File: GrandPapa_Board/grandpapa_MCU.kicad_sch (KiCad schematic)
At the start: 19 parts, among them J6 Conn_02x06, U10 MCP2515, U8 PIC18F26K83, Y1 12MHz

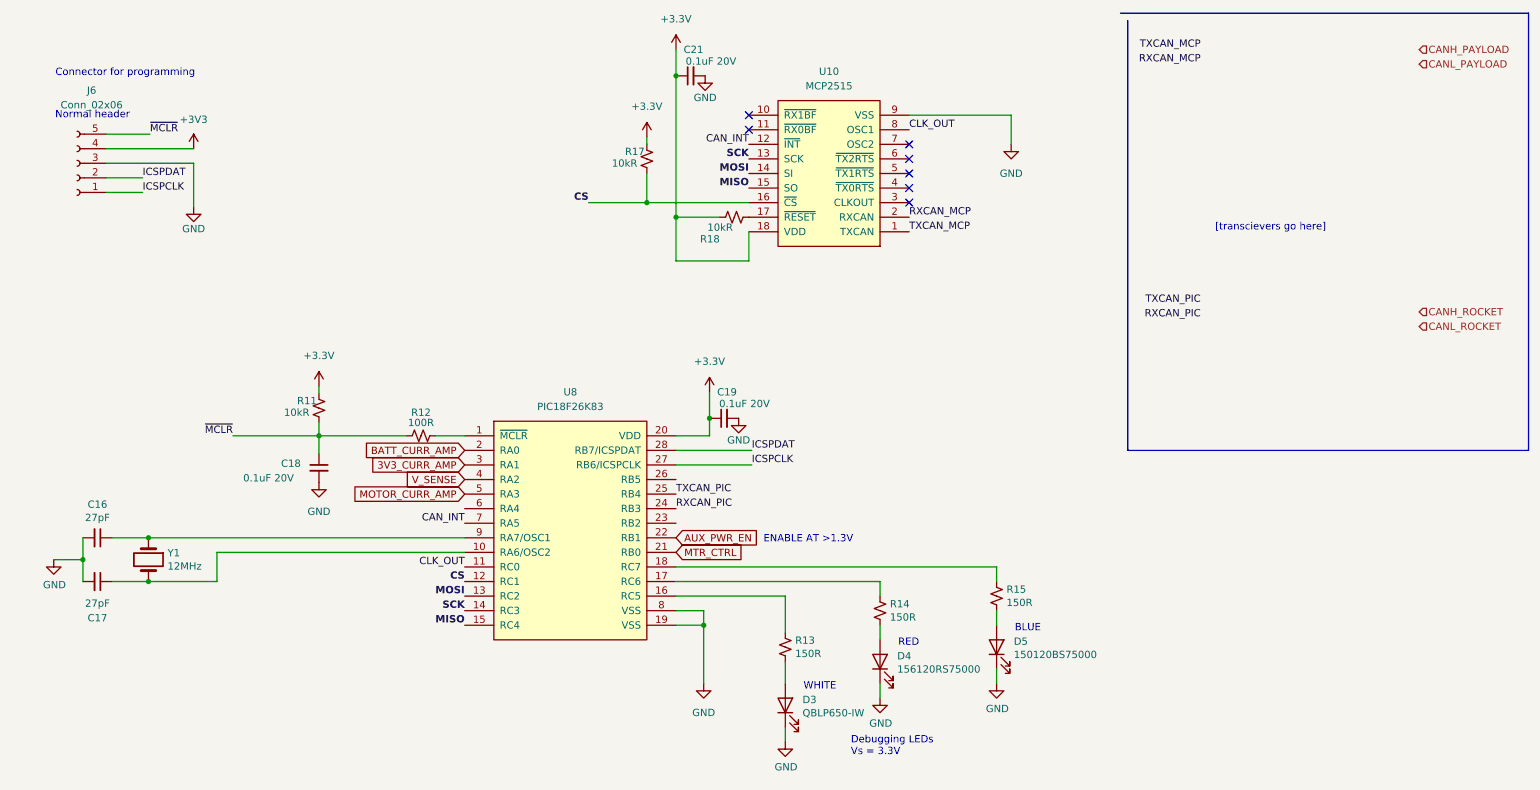
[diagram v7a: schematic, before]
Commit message: clean up schematic, edit nets for clarification, add gnd test points, edit load switching scheme
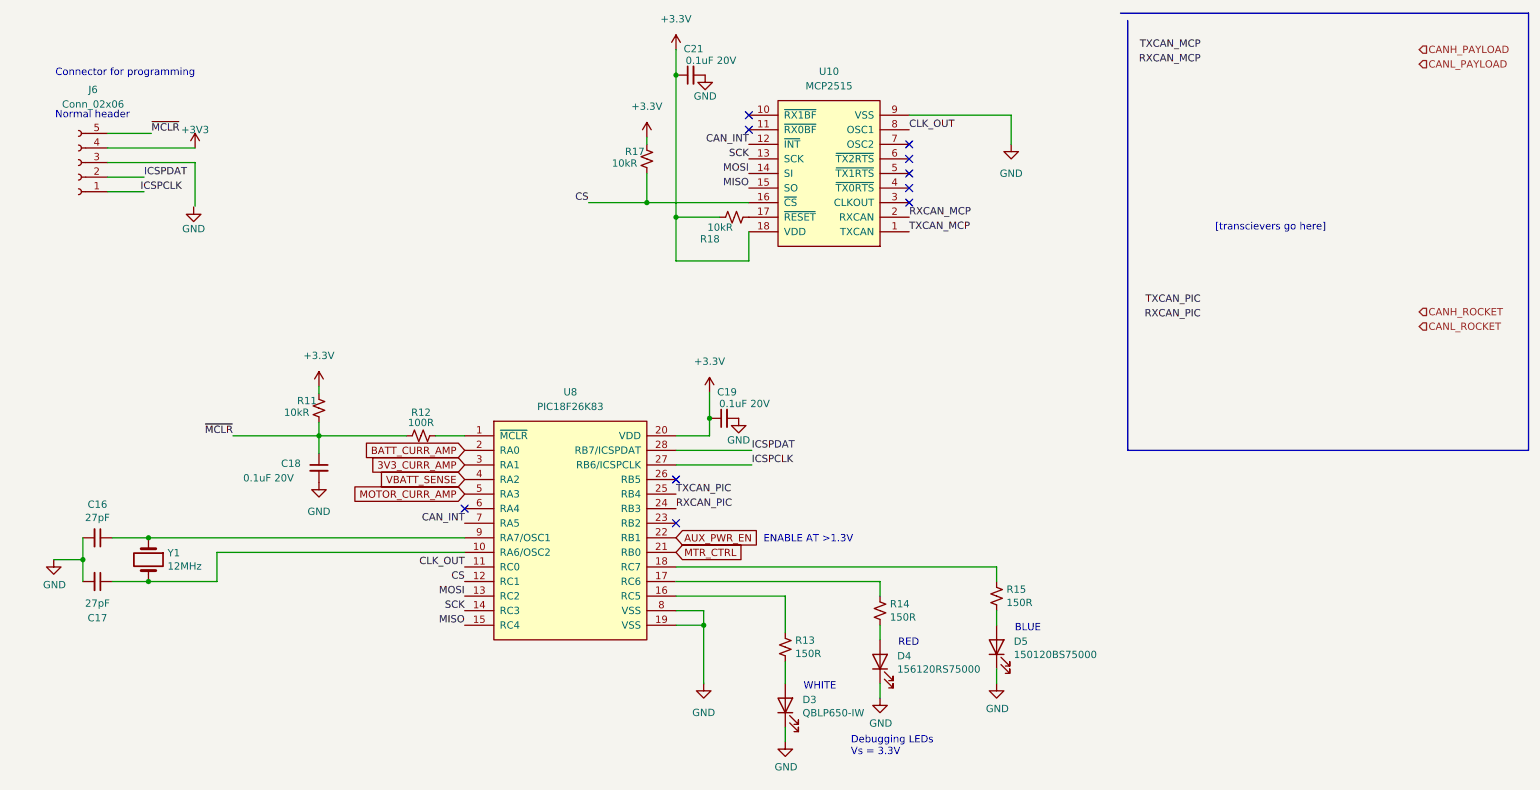
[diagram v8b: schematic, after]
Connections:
- net GND: no longer J6.3 (Pin_3)
- net V_SENSE renamed VBATT_SENSE
- no-connect marks 7 -> 10
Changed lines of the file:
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@@
   (junction (at 137.922 98.552) (diameter 0) (color 0 0 0 0)
   )
-  (junction (at 132.08 38.862) (diameter 0) (color 0 0 0 0)
+  (junction (at 132.08 38.735) (diameter 0) (color 0 0 0 0)
   )
   (junction (at 69.85 101.6) (diameter 0) (color 0 0 0 0)
@@
   (no_connect (at 172.72 58.42))
   (no_connect (at 172.72 60.96))
+  (no_connect (at 132.08 109.22))
+  (no_connect (at 132.08 116.84))
+  (no_connect (at 95.25 114.3))
   (wire (pts (xy 69.85 92.964) (xy 69.85 94.234))
     (stroke (width 0) (type default) (color 0 0 0 0))
@@
     (stroke (width 0) (type default) (color 0 0 0 0))
   )
-  (wire (pts (xy 32.766 49.022) (xy 40.386 49.022))
+  (wire (pts (xy 33.02 48.895) (xy 40.64 48.895))
     (stroke (width 0) (type default) (color 0 0 0 0))
   )
@@
     (stroke (width 0) (type default) (color 0 0 0 0))
   )
-  (wire (pts (xy 32.766 59.182) (xy 39.116 59.182))
+  (wire (pts (xy 33.02 59.055) (xy 39.37 59.055))
     (stroke (width 0) (type default) (color 0 0 0 0))
   )
@@
     (stroke (width 0) (type default) (color 0 0 0 0))
   )
-  (wire (pts (xy 32.766 56.642) (xy 39.116 56.642))
+  (wire (pts (xy 33.02 56.515) (xy 39.37 56.515))
     (stroke (width 0) (type default) (color 0 0 0 0))
   )
@@
     (stroke (width 0) (type default) (color 0 0 0 0))
   )
-  (wire (pts (xy 132.08 38.862) (xy 132.08 63.5))
+  (wire (pts (xy 132.08 38.735) (xy 132.08 63.5))
     (stroke (width 0) (type default) (color 0 0 0 0))
   )
@@
     (stroke (width 0) (type default) (color 0 0 0 0))
   )
-  (wire (pts (xy 48.006 54.102) (xy 48.006 61.722))
+  (wire (pts (xy 48.26 53.975) (xy 48.26 61.595))
     (stroke (width 0) (type default) (color 0 0 0 0))
   )
@@
     (stroke (width 0) (type default) (color 0 0 0 0))
   )
-  (wire (pts (xy 132.08 34.29) (xy 132.08 38.862))
-    (stroke (width 0) (type default) (color 0 0 0 0))
-  )
-  (wire (pts (xy 32.766 51.562) (xy 48.006 51.562))
+  (wire (pts (xy 132.08 34.29) (xy 132.08 38.735))
+    (stroke (width 0) (type default) (color 0 0 0 0))
+  )
+  (wire (pts (xy 33.02 51.435) (xy 48.26 51.435))
     (stroke (width 0) (type default) (color 0 0 0 0))
   )
@@
     (stroke (width 0) (type default) (color 0 0 0 0))
   )
-  (wire (pts (xy 32.766 54.102) (xy 48.006 54.102))
+  (wire (pts (xy 33.02 53.975) (xy 48.26 53.975))
     (stroke (width 0) (type default) (color 0 0 0 0))
   )
@@
   )
   (label "SCK" (at 144.78 53.34 180)
-    (effects (font (size 1.27 1.27) bold) (justify right bottom))
+    (effects (font (size 1.27 1.27)) (justify right bottom))
   )
   (label "TXCAN_MCP" (at 223.52 34.29 180)
@@
   )
   (label "MISO" (at 144.78 58.42 180)
-    (effects (font (size 1.27 1.27) bold) (justify right bottom))
+    (effects (font (size 1.27 1.27)) (justify right bottom))
   )
   (label "CLK_OUT" (at 172.72 48.26 0)
@@
   )
   (label "SCK" (at 95.25 132.08 180)
-    (effects (font (size 1.27 1.27) bold) (justify right bottom))
+    (effects (font (size 1.27 1.27)) (justify right bottom))
   )
   (label "RXCAN_PIC" (at 223.52 81.28 180)
     (effects (font (size 1.27 1.27)) (justify right bottom))
   )
-  (label "ICSPDAT" (at 39.116 56.642 0)
+  (label "ICSPDAT" (at 39.37 56.515 0)
     (effects (font (size 1.27 1.27)) (justify left bottom))
   )
@@
     (effects (font (size 1.27 1.27)) (justify left bottom))
   )
-  (label "~{MCLR}" (at 40.386 49.022 0)
+  (label "~{MCLR}" (at 40.64 48.895 0)
     (effects (font (size 1.27 1.27)) (justify left bottom))
   )
@@
   )
   (label "CS" (at 95.25 127 180)
-    (effects (font (size 1.27 1.27) bold) (justify right bottom))
+    (effects (font (size 1.27 1.27)) (justify right bottom))
   )
   (label "CAN_INT" (at 95.25 116.84 180)
     (effects (font (size 1.27 1.27)) (justify right bottom))
   )
-  (label "ICSPCLK" (at 39.116 59.182 0)
+  (label "ICSPCLK" (at 38.735 59.055 0)
     (effects (font (size 1.27 1.27)) (justify left bottom))
   )
   (label "MOSI" (at 95.25 129.54 180)
-    (effects (font (size 1.27 1.27) bold) (justify right bottom))
+    (effects (font (size 1.27 1.27)) (justify right bottom))
   )
   (label "CS" (at 116.84 60.96 180)
-    (effects (font (size 1.27 1.27) bold) (justify right bottom))
+    (effects (font (size 1.27 1.27)) (justify right bottom))
   )
   (label "RXCAN_MCP" (at 223.52 36.83 180)
@@
   )
   (label "MOSI" (at 144.78 55.88 180)
-    (effects (font (size 1.27 1.27) bold) (justify right bottom))
+    (effects (font (size 1.27 1.27)) (justify right bottom))
   )
   (label "TXCAN_PIC" (at 132.08 111.76 0)
@@
   )
   (label "MISO" (at 95.25 134.62 180)
-    (effects (font (size 1.27 1.27) bold) (justify right bottom))
+    (effects (font (size 1.27 1.27)) (justify right bottom))
   )
   (label "ICSPDAT" (at 145.288 104.14 0)
@@
     (effects (font (size 1.27 1.27)) (justify right bottom))
   )
-  (global_label "V_SENSE" (shape input) (at 95.25 109.22 180) (fields_autoplaced)
+  (global_label "VBATT_SENSE" (shape input) (at 95.25 109.22 180) (fields_autoplaced)
     (effects (font (size 1.27 1.27)) (justify right))
-    (property "Intersheet References" "${INTERSHEET_REFS}" (id 0) (at 224.79 210.82 0)
-      (effects (font (size 1.27 1.27)) hide)
+    (property "Intersheet References" "${INTERSHEET_REFS}" (id 0) (at 80.4393 109.1406 0)
+      (effects (font (size 1.27 1.27)) (justify right) hide)
     )
   )
@@
     (pin "2")
   )
-  (symbol (lib_id "Device:C_Small") (at 134.62 38.862 90) (unit 1)
-    (in_bom yes) (on_board yes)
-    (property "Reference" "C21" (id 0) (at 135.128 34.29 90))
-    (property "Value" "0.1uF 20V" (id 1) (at 138.176 36.322 90))
-    (property "Footprint" "" (id 2) (at 134.62 38.862 0)
-      (effects (font (size 1.27 1.27)) hide)
-    )
-    (property "Datasheet" "~" (id 3) (at 134.62 38.862 0)
+  (symbol (lib_id "Device:C_Small") (at 134.62 38.735 90) (unit 1)
+    (in_bom yes) (on_board yes)
+    (property "Reference" "C21" (id 0) (at 135.128 34.163 90))
+    (property "Value" "0.1uF 20V" (id 1) (at 138.176 36.195 90))
+    (property "Footprint" "" (id 2) (at 134.62 38.735 0)
+      (effects (font (size 1.27 1.27)) hide)
+    )
+    (property "Datasheet" "~" (id 3) (at 134.62 38.735 0)
       (effects (font (size 1.27 1.27)) hide)
     )
@@
     (pin "1")
   )
-  (symbol (lib_id "power:GND") (at 137.16 38.862 0) (unit 1)
-    (in_bom yes) (on_board yes)
-    (property "Reference" "#PWR0110" (id 0) (at 137.16 45.212 0)
-      (effects (font (size 1.27 1.27)) hide)
-    )
-    (property "Value" "GND" (id 1) (at 137.16 42.672 0))
-    (property "Footprint" "" (id 2) (at 137.16 38.862 0)
-      (effects (font (size 1.27 1.27)) hide)
-    )
-    (property "Datasheet" "" (id 3) (at 137.16 38.862 0)
+  (symbol (lib_id "power:GND") (at 137.16 38.735 0) (unit 1)
+    (in_bom yes) (on_board yes)
+    (property "Reference" "#PWR0110" (id 0) (at 137.16 45.085 0)
+      (effects (font (size 1.27 1.27)) hide)
+    )
+    (property "Value" "GND" (id 1) (at 137.16 42.418 0))
+    (property "Footprint" "" (id 2) (at 137.16 38.735 0)
+      (effects (font (size 1.27 1.27)) hide)
+    )
+    (property "Datasheet" "" (id 3) (at 137.16 38.735 0)
       (effects (font (size 1.27 1.27)) hide)
     )
@@
     (pin "2")
   )
-  (symbol (lib_id "Connector:Conn_01x05_Female") (at 27.686 54.102 180) (unit 1)
-    (in_bom yes) (on_board yes)
-    (property "Reference" "J6" (id 0) (at 30.226 41.402 0))
-    (property "Value" "Conn_02x06" (id 1) (at 30.226 43.942 0))
-    (property "Footprint" "Connector_PinHeader_2.54mm:PinHeader_1x05_P2.54mm_Vertical" (id 2) (at 27.686 54.102 0)
-      (effects (font (size 1.27 1.27)) hide)
-    )
-    (property "Datasheet" "~" (id 3) (at 27.686 54.102 0)
+  (symbol (lib_id "Connector:Conn_01x05_Female") (at 27.94 53.975 180) (unit 1)
+    (in_bom yes) (on_board yes)
+    (property "Reference" "J6" (id 0) (at 30.48 41.275 0))
+    (property "Value" "Conn_02x06" (id 1) (at 30.48 43.815 0))
+    (property "Footprint" "Connector_PinHeader_2.54mm:PinHeader_1x05_P2.54mm_Vertical" (id 2) (at 27.94 53.975 0)
+      (effects (font (size 1.27 1.27)) hide)
+    )
+    (property "Datasheet" "~" (id 3) (at 27.94 53.975 0)
       (effects (font (size 1.27 1.27)) hide)
     )
@@
     (pin "2")
   )
-  (symbol (lib_id "power:+3V3") (at 48.006 51.562 0) (unit 1)
-    (in_bom yes) (on_board yes) (fields_autoplaced)
-    (property "Reference" "#PWR0107" (id 0) (at 48.006 55.372 0)
-      (effects (font (size 1.27 1.27)) hide)
-    )
-    (property "Value" "+3V3" (id 1) (at 48.006 46.482 0))
-    (property "Footprint" "" (id 2) (at 48.006 51.562 0)
-      (effects (font (size 1.27 1.27)) hide)
-    )
-    (property "Datasheet" "" (id 3) (at 48.006 51.562 0)
-      (effects (font (size 1.27 1.27)) hide)
-    )
+  (symbol (lib_id "power:+3V3") (at 48.26 51.435 0) (unit 1)
+    (in_bom yes) (on_board yes)
+    (property "Reference" "#PWR0107" (id 0) (at 48.26 55.245 0)
+      (effects (font (size 1.27 1.27)) hide)
+    )
+    (property "Value" "+3V3" (id 1) (at 48.26 48.26 0))
+    (property "Footprint" "" (id 2) (at 48.26 51.435 0)
+      (effects (font (size 1.27 1.27)) hide)
+    )
+    (property "Datasheet" "" (id 3) (at 48.26 51.435 0)
+      (effects (font (size 1.27 1.27)) hide)
+    )
